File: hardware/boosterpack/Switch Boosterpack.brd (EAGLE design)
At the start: 49.5 x 49.5 mm, 36 parts, among them IC1 LAUNCHPAD-50MM, Q1 IRFR3709, Q2 IRFR3709, Q3 IRFR3709, Q4 IRFR3709

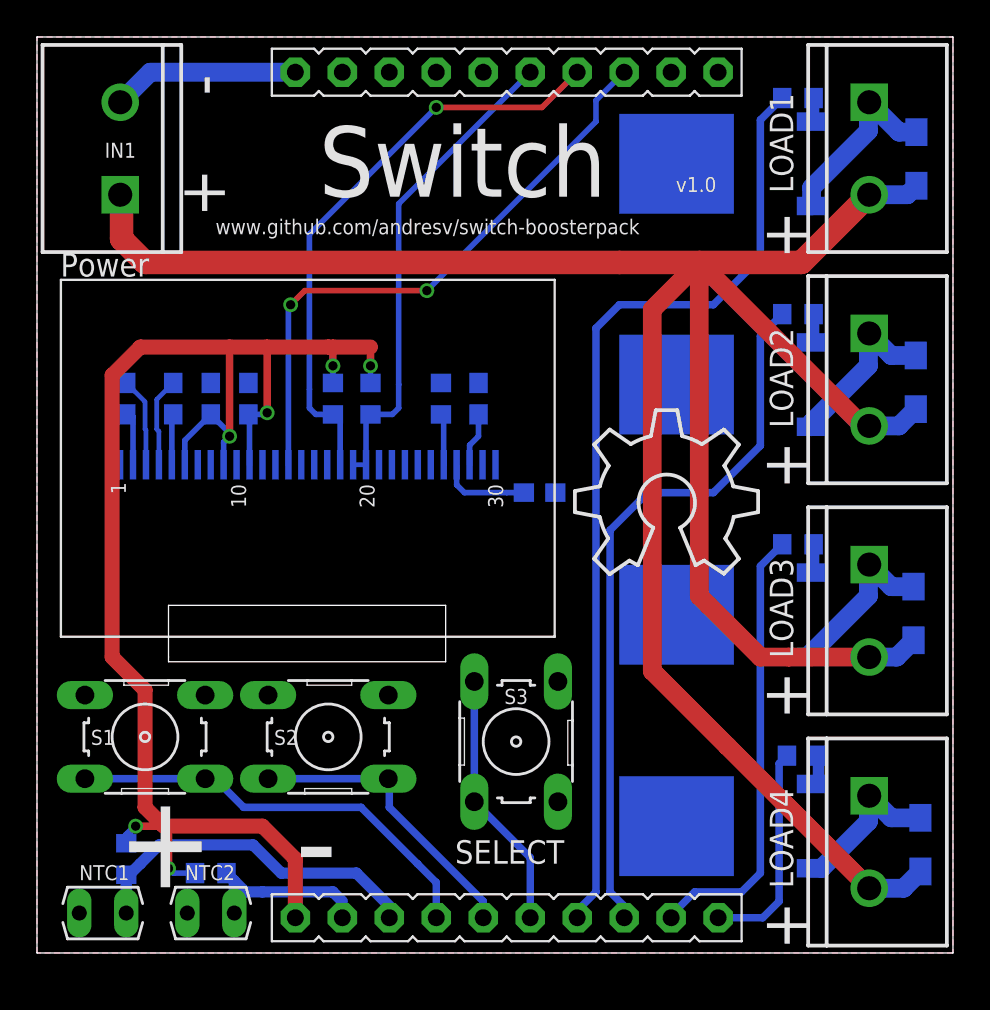
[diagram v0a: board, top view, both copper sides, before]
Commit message: Tweaked silkscreen and made OLED ribbon cutoff longer.
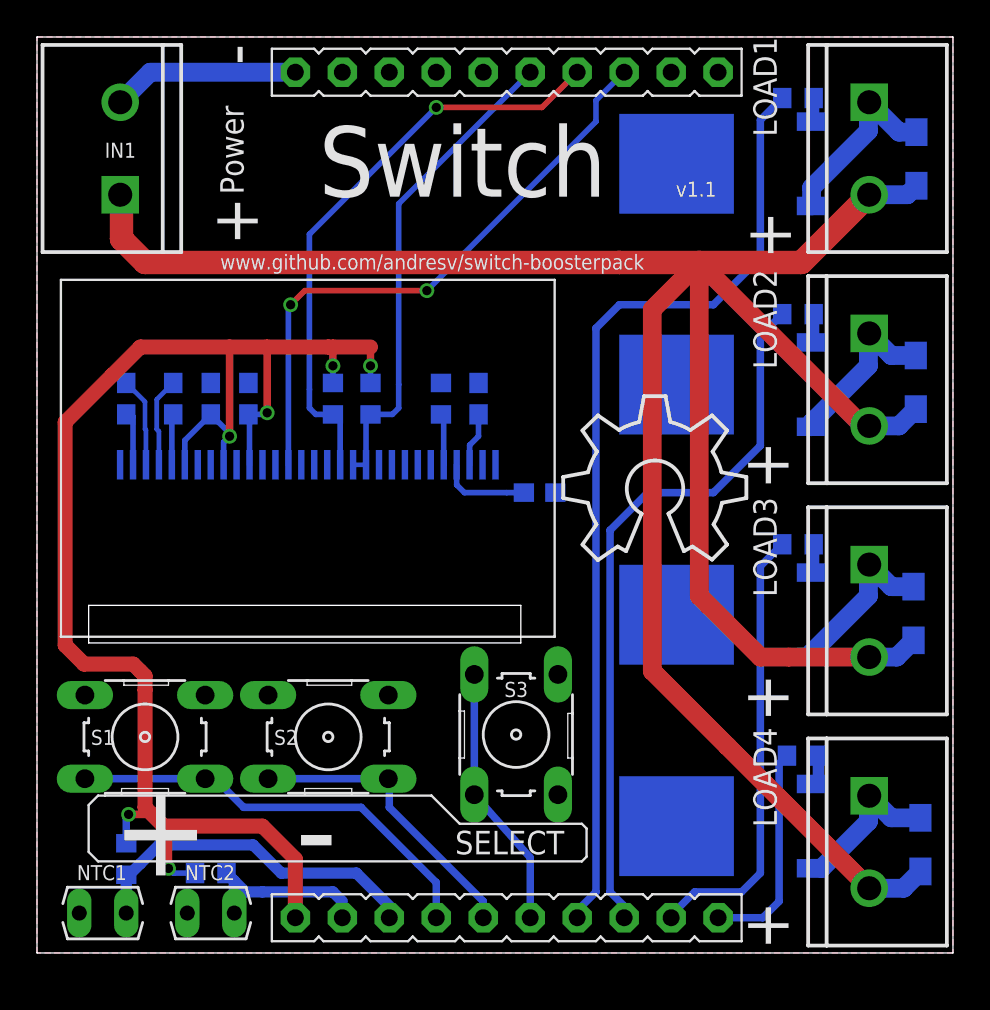
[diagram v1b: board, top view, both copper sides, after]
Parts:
- moved LOGO1 0.99 mm to (28.5, 21.2)
- moved S3 0.38 mm to (25.9, 11.8)
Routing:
- net +3V3: track 80.6 -> 85.3 mm
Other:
- board text added: "v1.1"
- board text removed: "v1.0"
